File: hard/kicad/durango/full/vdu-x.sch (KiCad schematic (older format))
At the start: 48 parts, among them J105 SCART, J4 LED, Q306 BC548, Q4 BC548, Q5 BC548, U124 74HC574, U125 74HC157, U126 HC86, U127 74HC245, U15 74HCT4040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

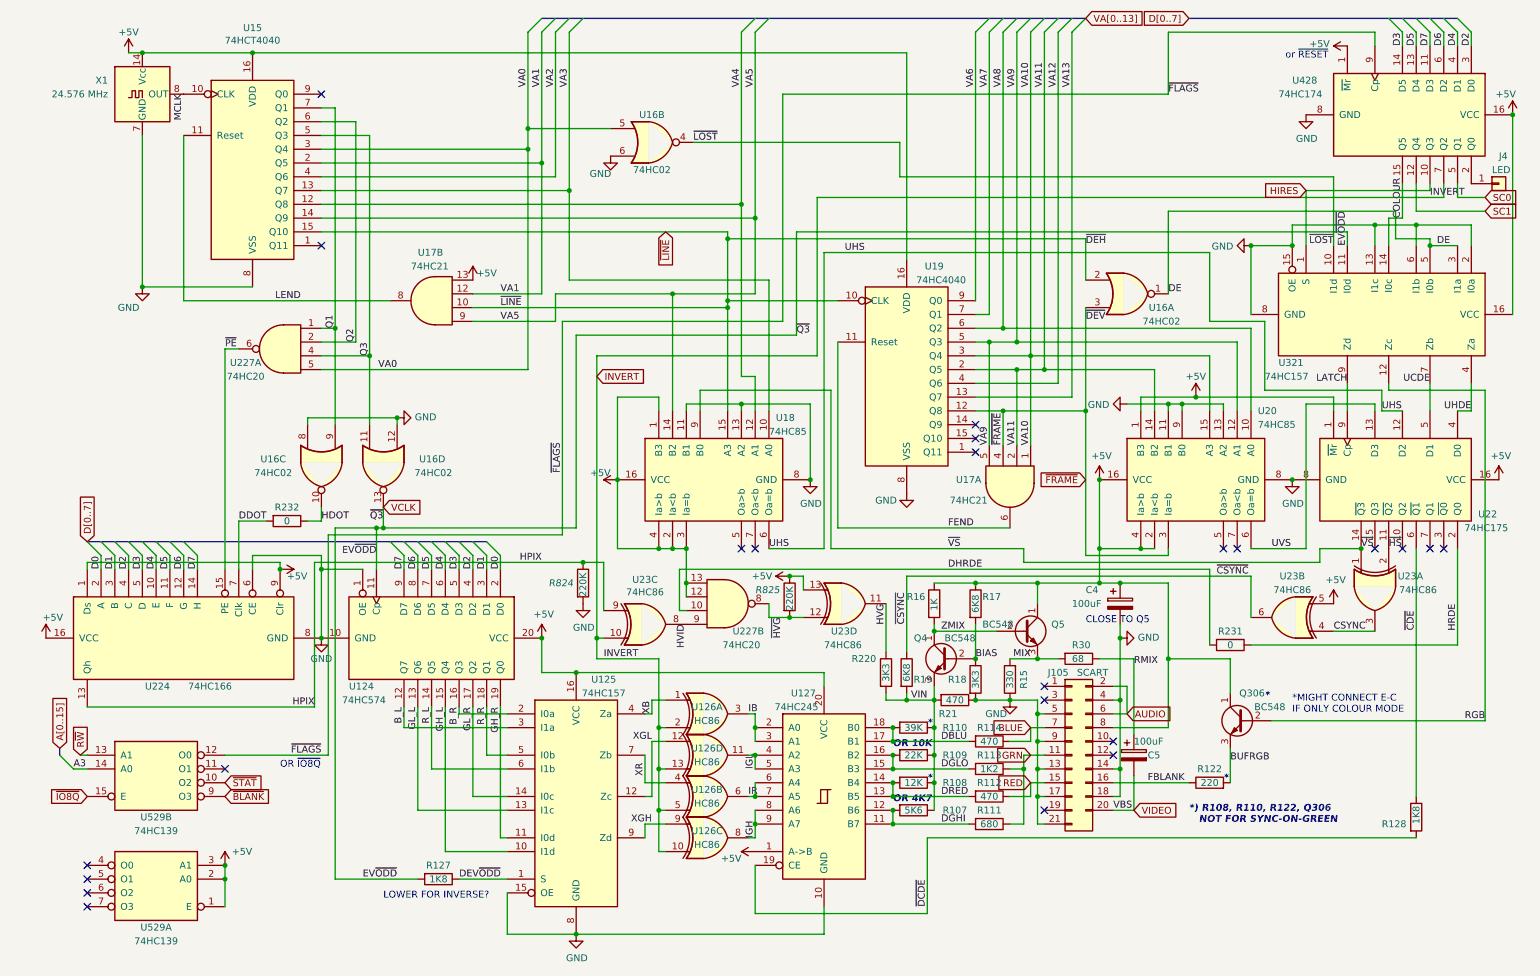
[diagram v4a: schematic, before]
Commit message: add tuning resistors to Durango-X
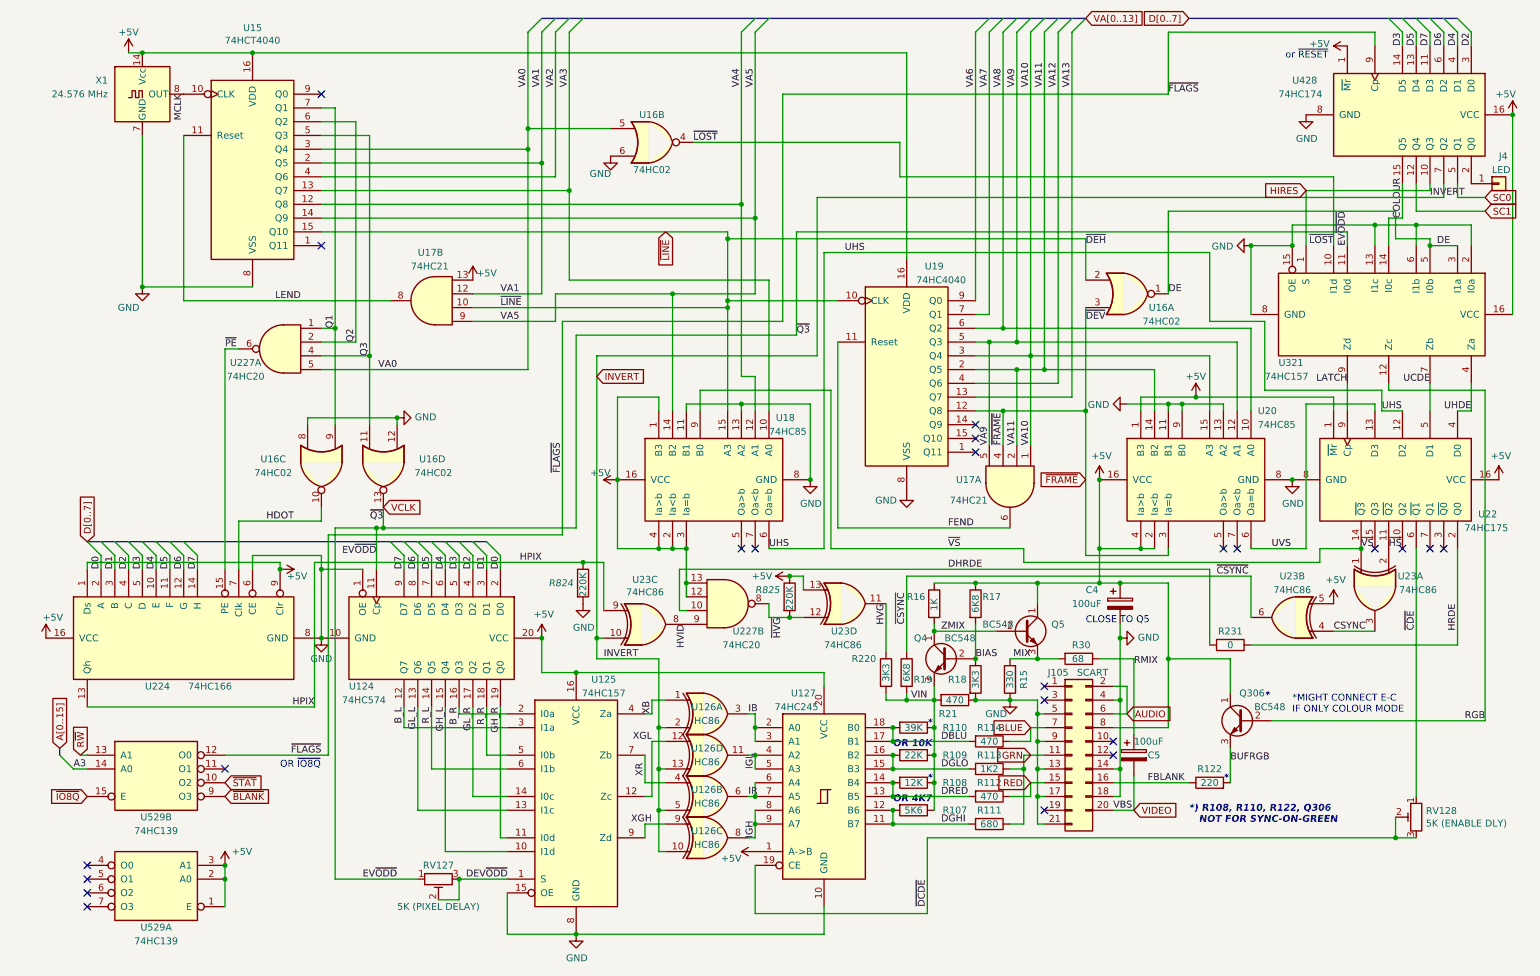
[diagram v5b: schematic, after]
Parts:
- removed R127, R128: 1K8, Resistor_THT:R_Axial_DIN0207_L6.3mm_D2.5mm_P2.54mm_Vertical, symbol Device:R
- removed R232: 0, Resistor_THT:R_Axial_DIN0207_L6.3mm_D2.5mm_P2.54mm_Vertical, symbol Device:R
- added RV127: 5K (PIXEL DELAY), Potentiometer_THT:Potentiometer_Piher_PT-10-V10_Vertical, symbol Device:R_POT_TRIM
- added RV128: 5K (ENABLE DLY), Potentiometer_THT:Potentiometer_Piher_PT-10-V10_Vertical, symbol Device:R_POT_TRIM
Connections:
- net DDOT is gone; now on net HDOT: U224.7 (Clk)
- net DEV~ODD: now also RV127.2, RV127.3
- net VCLK: now also RV127.1
- net ~CDE: now also RV128.1
- net ~DCDE: now also RV128.2, RV128.3
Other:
- note removed: "LOWER FOR INVERSE?"
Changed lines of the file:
@@
 	0    -1   -1   0
 $EndComp
-Text Label 2500 4200 0    50   ~ 0
+Text Label 2100 4200 0    50   ~ 0
 HDOT
 Wire Wire Line
@@
 Text Label 2800 6800 0    50   ~ 0
 EV~ODD
-$Comp
-L Device:R R127
-U 1 1 614B20D9
-P 3350 6800
-F 0 "R127" V 3250 6800 50  0000 C CNN
-F 1 "1K8" V 3350 6800 50  0000 C CNN
-F 2 "Resistor_THT:R_Axial_DIN0207_L6.3mm_D2.5mm_P2.54mm_Vertical" V 3280 6800 50  0001 C CNN
-F 3 "~" H 3350 6800 50  0001 C CNN
-	1    3350 6800
-	0    1    1    0
-$EndComp
 Wire Wire Line
 	6900 6500 6900 7050
-$Comp
-L Device:R R128
-U 1 1 615883A5
-P 10450 6350
-F 0 "R128" H 10200 6300 50  0000 L CNN
-F 1 "1K8" V 10450 6300 50  0000 L CNN
-F 2 "Resistor_THT:R_Axial_DIN0207_L6.3mm_D2.5mm_P2.54mm_Vertical" V 10380 6350 50  0001 C CNN
-F 3 "~" H 10450 6350 50  0001 C CNN
-	1    10450 6350
-	1    0    0    -1
-$EndComp
 Wire Wire Line
 	10450 6200 10450 4400
@@
 Wire Wire Line
 	3500 6800 3850 6800
-Text Label 3500 6800 0    50   ~ 0
+Text Label 3550 6800 0    50   ~ 0
 DEV~ODD
 Wire Wire Line
@@
 Wire Wire Line
 	10950 1950 10450 1950
-Text Notes 2950 6950 0    50   ~ 0
-LOWER FOR INVERSE?
 $Comp
 L power:+5V #PWR0151
@@
 Wire Wire Line
 	2600 2800 2600 3500
-$Comp
-L Device:R R232
-U 1 1 62770BF6
-P 2250 4200
-F 0 "R232" V 2150 4200 50  0000 C CNN
-F 1 "0" V 2250 4200 50  0000 C CNN
-F 2 "Resistor_THT:R_Axial_DIN0207_L6.3mm_D2.5mm_P2.54mm_Vertical" V 2180 4200 50  0001 C CNN
-F 3 "~" H 2250 4200 50  0001 C CNN
-	1    2250 4200
-	0    1    1    0
-$EndComp
-Wire Wire Line
-	2100 4200 1900 4200
-Wire Wire Line
-	2400 4200 2500 4200
 Wire Wire Line
 	2500 4200 2500 4100
@@
 Text Label 5650 6500 1    50   ~ 0
 IGH
-Text Label 1900 4200 0    50   ~ 0
-DDOT
 Text Label 8400 5250 0    50   ~ 0
 RMIX
@@
 	8300 5050 8300 5500
 Wire Wire Line
-	6900 6500 10450 6500
+	6900 6500 10300 6500
 Wire Wire Line
 	8400 6100 8400 6300
@@
 	3600 2750 4200 2750
 Connection ~ 5050 2550
-Wire Bus Line
-	8800 550  10750 550
-Wire Bus Line
-	4100 550  8050 550
-Wire Bus Line
-	800  4350 3700 4350
 Text Label 7650 3650 1    50   ~ 0
 VA10
@@
 Text Label 7350 3650 1    50   ~ 0
 VA9
+Wire Wire Line
+	1900 4200 2500 4200
+$Comp
+L Device:R_POT_TRIM RV127
+U 1 1 628F2E8C
+P 3350 6800
+F 0 "RV127" V 3250 6800 50  0000 C CNN
+F 1 "5K (PIXEL DELAY)" V 3550 6800 50  0000 C CNN
+F 2 "Potentiometer_THT:Potentiometer_Piher_PT-10-V10_Vertical" H 3350 6800 50  0001 C CNN
+F 3 "~" H 3350 6800 50  0001 C CNN
+	1    3350 6800
+	0    -1   1    0
+$EndComp
+$Comp
+L Device:R_POT_TRIM RV128
+U 1 1 6292D03A
+P 10450 6350
+F 0 "RV128" H 10380 6396 50  0000 R CNN
+F 1 "5K (ENABLE DLY)" H 10380 6305 50  0000 R CNN
+F 2 "Potentiometer_THT:Potentiometer_Piher_PT-10-V10_Vertical" H 10450 6350 50  0001 C CNN
+F 3 "~" H 10450 6350 50  0001 C CNN
+	1    10450 6350
+	-1   0    0    -1
+$EndComp
+Wire Wire Line
+	3350 6950 3500 6950
+Wire Wire Line
+	3500 6950 3500 6800
+Connection ~ 3500 6800
+Wire Wire Line
+	10300 6350 10300 6500
+Wire Bus Line
+	8800 550  10750 550
+Wire Bus Line
+	4100 550  8050 550
+Wire Bus Line
+	800  4350 3700 4350
+Connection ~ 10300 6500
+Wire Wire Line
+	10300 6500 10450 6500
 $EndSCHEMATC

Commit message: remove duplicate names on signals
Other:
- note added: "= ~DEH"
- note added: "= ~DEV"
- note added: "=EV~ODD"
- note added: "EV~ODD"
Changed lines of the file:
@@
 Text Label 9400 4400 0    50   ~ 0
 UVS
-Text Label 8050 2200 0    50   ~ 0
-~DEH
-Text Label 8050 2750 0    50   ~ 0
-~DEV
 Wire Wire Line
 	8050 3400 8050 2650
@@
 P 8350 3350
 F 0 "#PWR0123" H 8350 3100 50  0001 C CNN
-F 1 "GND" V 8355 3222 50  0000 R CNN
+F 1 "GND" V 8450 3350 50  0000 R CNN
 F 2 "" H 8350 3350 50  0001 C CNN
 F 3 "" H 8350 3350 50  0001 C CNN
@@
 Wire Wire Line
 	8650 1950 8650 2550
-Text Label 2950 4200 2    50   ~ 0
-~Q3
 Wire Wire Line
 	2950 4250 4350 4250
 Wire Wire Line
 	4350 4250 4350 2850
-Text Label 5950 2850 0    50   ~ 0
-~Q3
+Text Label 5850 2850 0    50   ~ 0
+VCLK
 Text Label 6900 7000 1    50   ~ 0
 ~DCDE
@@
 Wire Wire Line
 	9550 2200 9550 2050
-Text Label 9950 2200 1    50   ~ 0
-EV~ODD
 Text Label 9850 2200 2    50   ~ 0
 ~LOST
@@
 Text GLabel 2950 4100 2    50   Input ~ 0
 VCLK
-Text Label 2800 6800 0    50   ~ 0
-EV~ODD
 Wire Wire Line
 	6900 6500 6900 7050
@@
 Text Notes 9050 6100 0    50   Italic 10
 *
-Text Label 8250 6300 0    50   ~ 0
-VBS
 $Comp
 L Device:R R107
@@
 Text GLabel 750  5900 1    50   Input ~ 0
 R~W
-Text Label 2900 4450 2    50   ~ 0
-EV~ODD
 $Comp
 L Connector_Generic:Conn_01x01 J4
@@
 Wire Wire Line
 	8400 6050 8400 6100
-Wire Wire Line
-	8400 6300 8250 6300
 Wire Wire Line
 	8250 6100 8800 6100
@@
 Wire Wire Line
 	10300 6350 10300 6500
+Connection ~ 10300 6500
+Wire Wire Line
+	10300 6500 10450 6500
 Wire Bus Line
 	8800 550  10750 550
@@
 Wire Bus Line
 	800  4350 3700 4350
-Connection ~ 10300 6500
-Wire Wire Line
-	10300 6500 10450 6500
+Text Notes 3000 4250 0    50   ~ 0
+=EV~ODD
+Text Notes 2650 6800 0    50   ~ 0
+=EV~ODD
+Text Notes 8050 2200 0    50   ~ 0
+= ~DEH
+Text Notes 8050 3250 0    50   ~ 0
+= ~DEV
+Text Notes 9950 2250 1    50   ~ 0
+EV~ODD
+Wire Wire Line
+	8400 6300 8250 6300
 $EndSCHEMATC
